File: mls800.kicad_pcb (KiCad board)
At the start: 2 copper layers, 293.4 x 80.5 mm, 106 parts, among them CON1 BARREL_JACK, IC1 6N137, J1 USB, J10 NSJ8HC, J11 NRJ4HF-1, J2 NRJ4HF-1, J3 NSJ8HC, J4 NSJ8HC, J5 NSJ8HC, J6 NSJ8HC, J7 NSJ8HC, J8 NSJ8HC, J9 NSJ8HC, P1 CONN_02X03, P2 DIN_5, P3 DIN_5, P4 CONN_02X03, P5 CONN_02X03, SW10 SW_TACT_LED, SW11 SW_TACT_LED, SW12 SW_PUSH, SW2 SW_TACT_LED, SW3 SW_TACT_LED, SW4 SW_TACT_LED, SW5 SW_TACT_LED, SW6 SW_TACT_LED, SW7 SW_TACT_LED, SW8 SW_TACT_LED, SW9 SW_TACT_LED, U1 LM340MP-5.0/NOPB, U2 ATmega32U4-AU, U3 24LC256, U4 MCP23017, U5 AS1115, U6 ULN2803A, U7 ULN2803A, U8 LM340MP-5.0/NOPB, X1 16Mhz

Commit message: Ordered PCB (with one major mistake : the two 22R are two small to dissipate 3W !!)
BOM filling
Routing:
- net /Front panel/DGND: track 18.6 -> 31.3 mm, vias 4 -> 6
- net GND: track 237.5 -> 246.2 mm, vias 29 -> 31
- net +5V: track 348.9 -> 350.1 mm
- net /RESET: track 33.9 -> 34.6 mm
- net Net-(RE7-Pad10): track 43.0 -> 43.5 mm
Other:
- board text added: "Edit"
- board text added: "Exit/Menu"
- board text added: "France 2015"
- board text added: "ICSP"
- board text added: "In"
- board text added: "MLS800 Rev. A"
- board text added: "Out"
- board text added: "Reset"
- board text added: "Rx"
- board text added: "Tx"

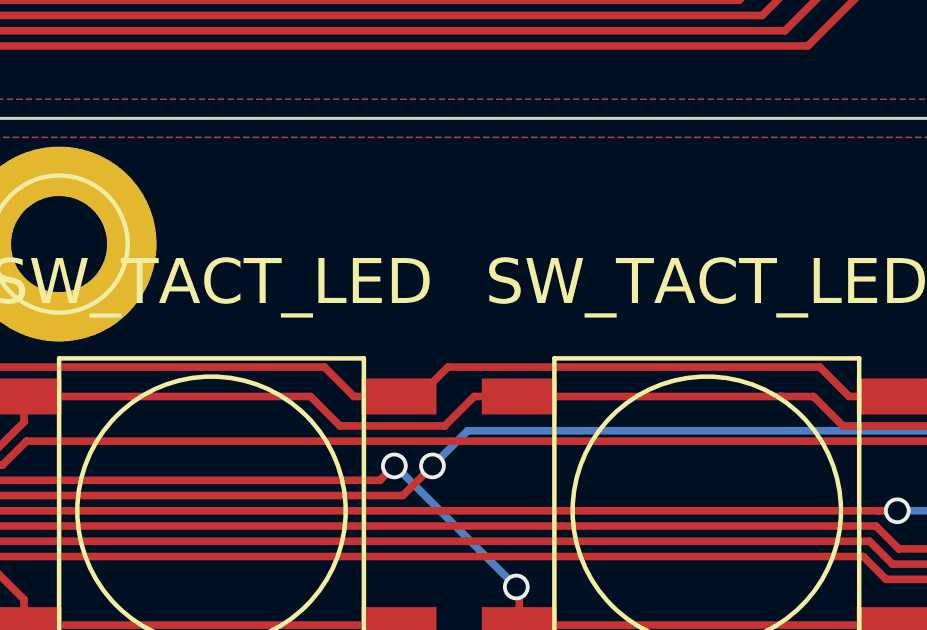
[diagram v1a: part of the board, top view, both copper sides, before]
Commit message: Fixed silkscreen for up/down buttons
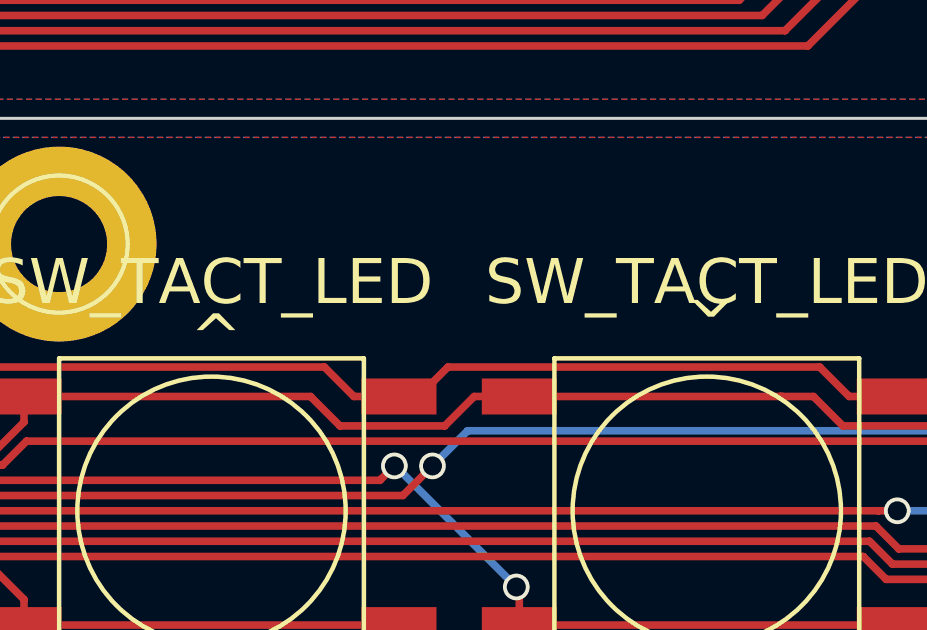
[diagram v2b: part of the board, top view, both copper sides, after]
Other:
- board text added: "^"
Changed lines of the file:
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@@
     (area 27.94 31.440001 350.9 125.780001)
     (thickness 1.6)
-    (drawings 33)
+    (drawings 35)
     (tracks 1434)
     (zones 0)
@@
     (solder_mask_min_width 0.1)
     (aux_axis_origin 0 0)
-    (visible_elements 7FFEFF7F)
+    (visible_elements 7FFEFFFF)
     (pcbplotparams
       (layerselection 0x010f0_80000001)
@@
     )
   )
+  (gr_text ^ (at 213.5 105.5 180) (layer F.SilkS)
+    (effects (font (size 1.5 1.5) (thickness 0.3)))
+  )
+  (gr_text ^ (at 197 107) (layer F.SilkS)
+    (effects (font (size 1.5 1.5) (thickness 0.3)))
+  )
   (gr_text . (at 120.65 122.555) (layer F.SilkS)

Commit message: Imported new netlist
Deleted wrong tracks
Re arrange basic footprints
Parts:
- C15, C19: footprint Capacitors_SMD:C_0805_HandSoldering -> Capacitors_SMD:c_elec_6.3x7.7
- C4, C5, C9: value 100nF -> 0.1uF
- C8: footprint Capacitors_Tantalum_SMD:TantalC_SizeA_EIA-3216_HandSoldering -> Capacitors_SMD:C_0805_HandSoldering
- D1, D5: value CD1206-S01575 -> 1N4148; footprint SMD_Packages:SMD-1206_Pol -> Custom-device:SOD-123_Handsoldering
- P1, P4, P5: footprint Pin_Headers:Pin_Header_Straight_2x03 -> Custom-conn:VASCH3x2
- R19: value R -> 23.6k
- R5, R8: value 10K -> 1k
- moved C20 5.08 mm to (237.5, 87.6)
- moved C19 3.59 mm to (232.4, 90.2), turned to 90 degrees
- moved D5 2.54 mm to (262.9, 69.8), turned to 0 degrees
- moved R15 2.54 mm to (262.9, 67.3)
- turned D1 to 270 degrees
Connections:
- RE1 pad 10: Net-(RE1-Pad10) -> Net-(J2-Pad1)
- RE1 pad 3: Net-(J3-Pad6) -> GNDA
- RE1 pad 4: GNDA -> Net-(J3-Pad6)
- RE1 pad 9: Net-(J2-Pad1) -> Net-(RE1-Pad9)
- RE2 pad 10: Net-(RE2-Pad10) -> Net-(RE1-Pad9)
- RE2 pad 3: Net-(J4-Pad6) -> GNDA
- RE2 pad 4: GNDA -> Net-(J4-Pad6)
- RE2 pad 5: Net-(RE1-Pad10) -> Net-(RE1-Pad9)
- RE2 pad 9: Net-(RE1-Pad10) -> Net-(RE2-Pad9)
- RE3 pad 10: Net-(RE3-Pad10) -> Net-(RE2-Pad9)
- RE3 pad 3: Net-(J5-Pad6) -> GNDA
- RE3 pad 4: GNDA -> Net-(J5-Pad6)
- RE3 pad 5: Net-(RE2-Pad10) -> Net-(RE2-Pad9)
- RE3 pad 9: Net-(RE2-Pad10) -> Net-(RE3-Pad9)
- RE4 pad 10: Net-(RE4-Pad10) -> Net-(RE3-Pad9)
- RE4 pad 3: Net-(J6-Pad6) -> GNDA
- RE4 pad 4: GNDA -> Net-(J6-Pad6)
- RE4 pad 5: Net-(RE3-Pad10) -> Net-(RE3-Pad9)
- RE4 pad 9: Net-(RE3-Pad10) -> Net-(RE4-Pad9)
- RE5 pad 10: Net-(RE5-Pad10) -> Net-(RE4-Pad9)
- RE5 pad 3: Net-(J7-Pad6) -> GNDA
- RE5 pad 4: GNDA -> Net-(J7-Pad6)
- RE5 pad 5: Net-(RE4-Pad10) -> Net-(RE4-Pad9)
- RE5 pad 9: Net-(RE4-Pad10) -> Net-(RE5-Pad9)
- RE6 pad 10: Net-(RE6-Pad10) -> Net-(RE5-Pad9)
- RE6 pad 3: Net-(J8-Pad6) -> GNDA
- RE6 pad 4: GNDA -> Net-(J8-Pad6)
- RE6 pad 5: Net-(RE5-Pad10) -> Net-(RE5-Pad9)
- RE6 pad 9: Net-(RE5-Pad10) -> Net-(RE6-Pad9)
- RE7 pad 10: Net-(RE7-Pad10) -> Net-(RE6-Pad9)
- RE7 pad 3: Net-(J9-Pad6) -> GNDA
- RE7 pad 4: GNDA -> Net-(J9-Pad6)
- RE7 pad 5: Net-(RE6-Pad10) -> Net-(RE6-Pad9)
- RE7 pad 9: Net-(RE6-Pad10) -> Net-(RE7-Pad9)
- RE8 pad 10: Net-(J11-Pad1) -> Net-(RE7-Pad9)
- RE8 pad 3: Net-(J10-Pad6) -> GNDA
- RE8 pad 4: GNDA -> Net-(J10-Pad6)
- RE8 pad 5: Net-(RE7-Pad10) -> Net-(RE7-Pad9)
- RE8 pad 9: Net-(RE7-Pad10) -> Net-(J11-Pad1)
- SW11 pad 4: /Front panel/SEGF -> /Front panel/SEGD
- SW2 pad 3: /Front panel/SEGA -> /Front panel/SEGDP
- SW3 pad 3: /Front panel/SEGB -> /Front panel/SEGA
- SW4 pad 3: /Front panel/SEGC -> /Front panel/SEGB
- SW5 pad 3: /Front panel/SEGD -> /Front panel/SEGC
- SW6 pad 3: /Front panel/SEGE -> /Front panel/SEGD
- SW7 pad 3: /Front panel/SEGF -> /Front panel/SEGE
- SW8 pad 3: /Front panel/SEGG -> /Front panel/SEGF
- SW9 pad 3: /Front panel/SEGDP -> /Front panel/SEGG
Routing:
- net /Front panel/SEGF: track 241.4 -> 51.9 mm, vias 3 -> 0
- net /Front panel/SEGDP: track 204.6 -> 56.3 mm
- net /Front panel/SEGG: track 183.7 -> 46.4 mm, vias 2 -> 0
- net /Front panel/SEGE: track 202.8 -> 102.9 mm, vias 3 -> 1
- net /Front panel/SEGD: track 140.7 -> 59.9 mm
- net /Front panel/SEGC: track 119.3 -> 51.5 mm, vias 2 -> 0
- net GNDA: track 59.2 -> 4.36 mm, vias 8 -> 0
- net /Front panel/SEGB: track 98.2 -> 43.8 mm, vias 4 -> 2
- net Net-(RE6-Pad10): track 43.5 -> 0.00 mm
- net Net-(RE5-Pad10): track 43.5 -> 0.00 mm
- net Net-(RE7-Pad10): track 43.5 -> 0.00 mm
- net Net-(RE3-Pad10): track 43.3 -> 0.00 mm
- net Net-(RE2-Pad10): track 43.3 -> 0.00 mm
- net Net-(RE1-Pad10): track 43.3 -> 0.00 mm
- net Net-(RE4-Pad10): track 43.3 -> 0.00 mm
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
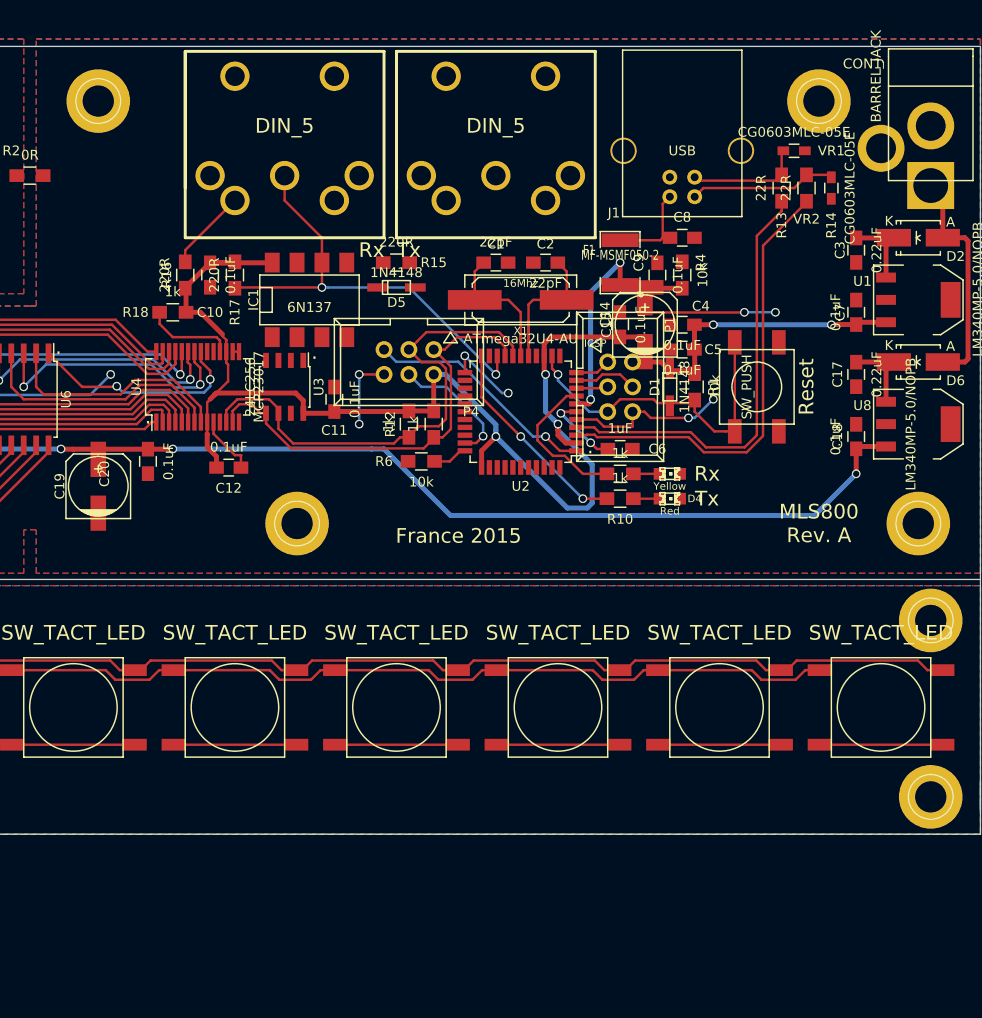
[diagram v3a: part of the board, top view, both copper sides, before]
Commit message: Started PCB Rev. A2 layout
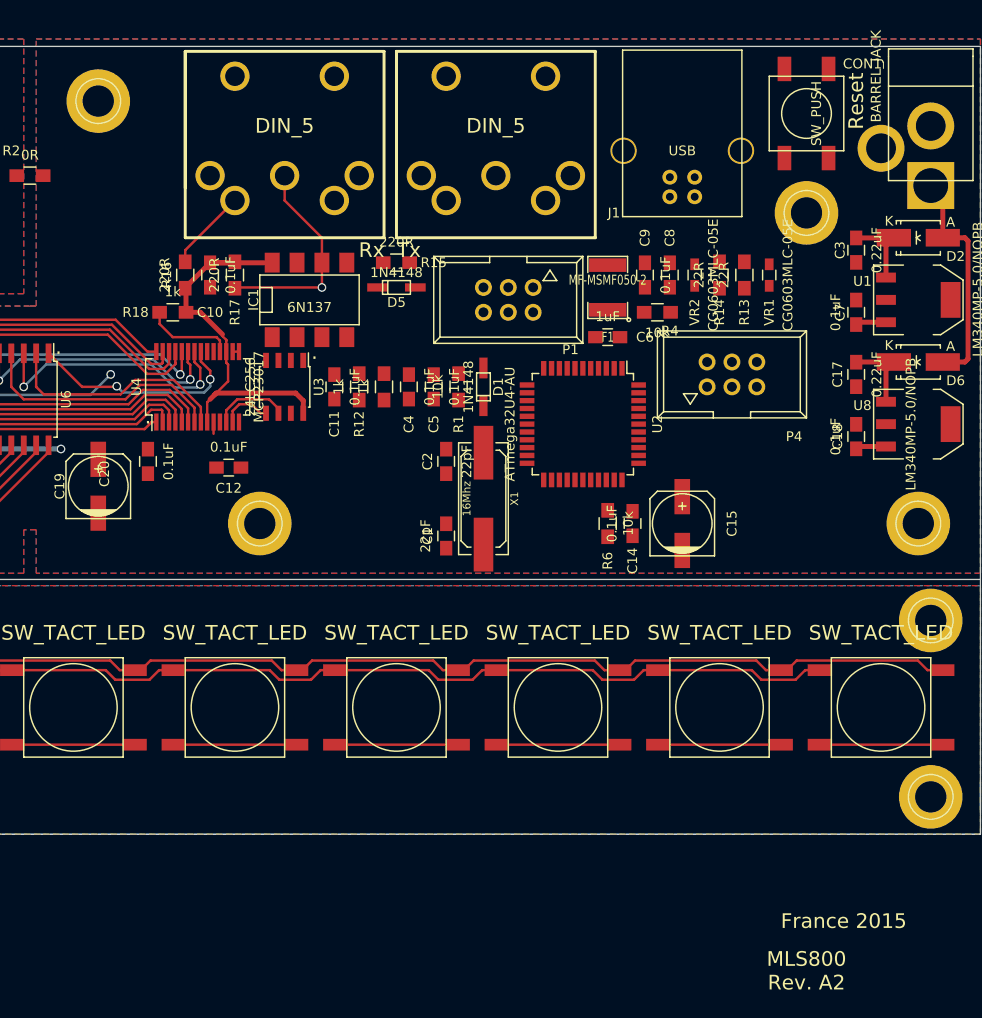
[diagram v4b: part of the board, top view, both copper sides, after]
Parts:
- removed D3: Yellow, LEDs:LED-0805
- removed D4: Red, LEDs:LED-0805
- removed R10, R9: 1k, Resistors_SMD:R_0805_HandSoldering
- moved P4 33.0 mm to (297.2, 78.7), turned to 0 degrees
- moved C4 28.7 mm to (264.2, 80.0), turned to 90 degrees
- moved SW12 28.4 mm to (304.8, 52.1), turned to 90 degrees
- moved C1 28.4 mm to (268.0, 95.2), turned to 270 degrees
- moved C5 25.7 mm to (266.7, 80.0), turned to 90 degrees
- moved R1 24.1 mm to (269.2, 80.0), turned to 270 degrees
- moved C2 22.7 mm to (268.0, 87.6), turned to 90 degrees
- moved C15 20.7 mm to (292.1, 94.0)
- moved X1 20.7 mm to (271.8, 91.4), turned to 270 degrees
- moved C14 20.4 mm to (287.0, 94.0), turned to 270 degrees
- moved R6 20.1 mm to (284.5, 94.0), turned to 90 degrees
- moved D1 19.1 mm to (271.8, 80.0), turned to 90 degrees
- moved VR2 16.6 mm to (293.4, 68.6)
- moved P1 14.5 mm to (274.3, 71.1), turned to 180 degrees
- moved VR1 13.0 mm to (301.0, 68.6), turned to 90 degrees
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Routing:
- net VCC: track 168.6 -> 44.0 mm, vias 7 -> 0
- net +5V: track 350.1 -> 261.7 mm, vias 19 -> 17
- net /D-: track 46.4 -> 0.00 mm
- net /D+: track 44.7 -> 0.00 mm
- net /Loops/SCL: track 51.0 -> 7.87 mm
- net /Loops/SDA: track 45.1 -> 5.21 mm
- net GND: track 234.1 -> 195.6 mm, vias 29 -> 23
- net /RESET: track 34.6 -> 0.00 mm, vias 1 -> 0
- net VCOM: track 25.8 -> 0.00 mm, vias 2 -> 0
- net /UI_INT: track 24.0 -> 0.00 mm, vias 1 -> 0
- net /RX: track 45.4 -> 22.0 mm, vias 2 -> 1
- net /TXLED: track 21.3 -> 0.00 mm, vias 2 -> 0
- net Net-(C2-Pad2): track 15.8 -> 0.00 mm
- net /RXLED: track 15.3 -> 0.00 mm
- net Net-(J1-Pad2): track 15.1 -> 0.00 mm
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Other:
- board text added: "MLS800 Rev. A2"
- board text removed: "ICSP"
- board text removed: "MLS800 Rev. A"

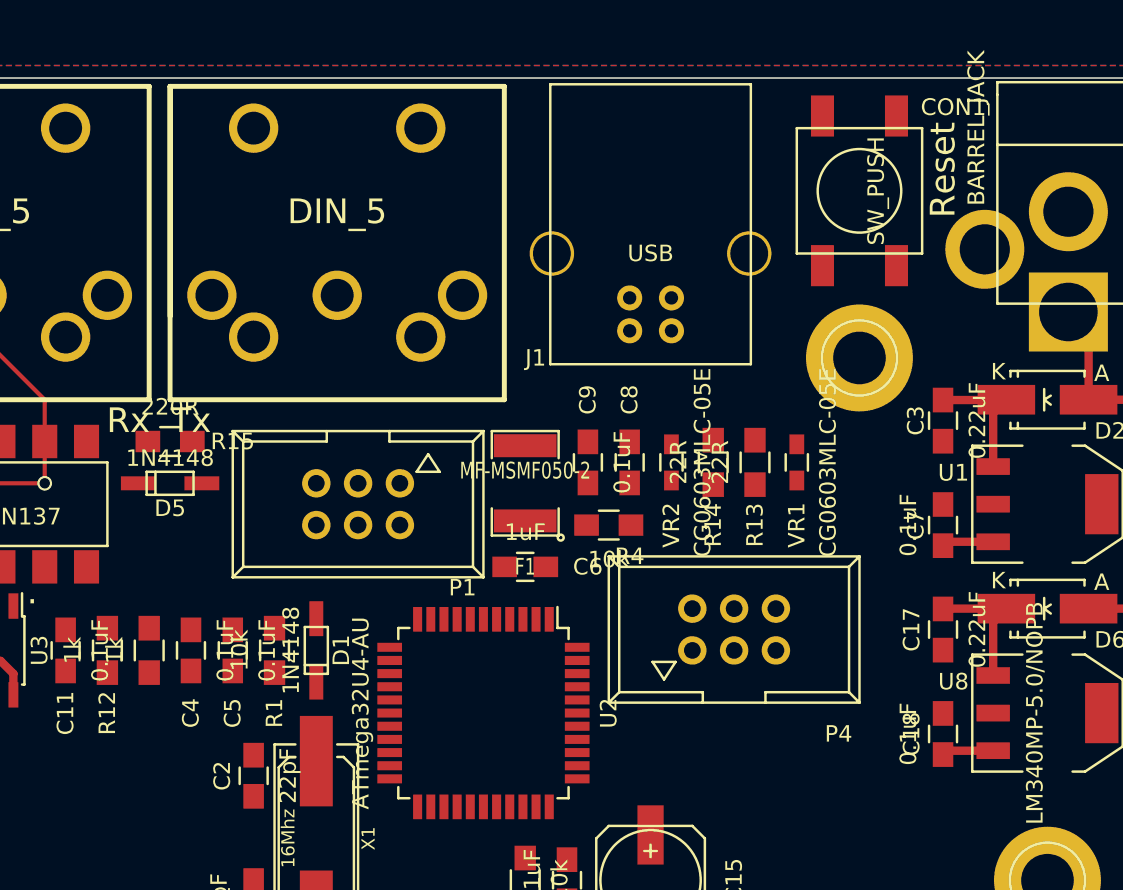
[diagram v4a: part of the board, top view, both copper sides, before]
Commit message: Added vertical push button component & footprint Updated pcb with that last footprint
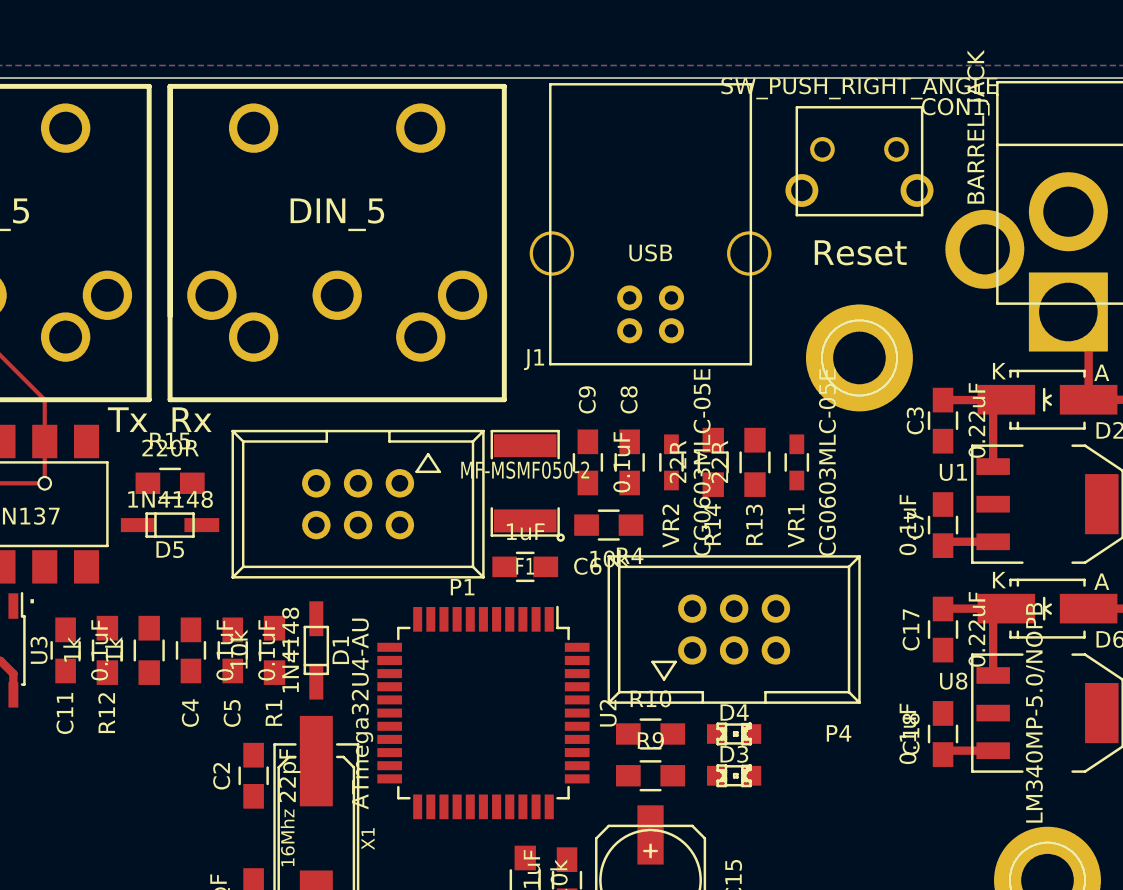
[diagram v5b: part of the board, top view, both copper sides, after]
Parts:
- added D3: Yellow, LEDs:LED-0805, F.Cu at (297.2, 87.6)
- added D4: Red, LEDs:LED-0805, F.Cu at (297.2, 85.1)
- added R10: 1k, Resistors_SMD:R_0805_HandSoldering, F.Cu at (292.1, 85.1)
- added R9: 1k, Resistors_SMD:R_0805_HandSoldering, F.Cu at (292.1, 87.6)
- SW12: value SW_PUSH -> SW_PUSH_RIGHT_ANGLE; footprint Custom-device:SW_PUSH_SMALL -> Custom-device:SW_PUSH_RIGHT_ANGLE
- moved D5 2.54 mm to (262.9, 72.4)
- moved R15 2.54 mm to (262.9, 69.8)
- moved SW12 1.27 mm to (304.8, 50.8), turned to 180 degrees
